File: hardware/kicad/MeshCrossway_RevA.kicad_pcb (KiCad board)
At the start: 2 copper layers, 0 parts

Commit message: Update Rev A KiCad PCB schematic and validated footprints
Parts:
- added BAT1: LiPo 3.7V 10000mAh 110x60x12, MeshCrossway:Battery_LiPo_10000mAh_110x60x12, B.Cu at (157.2, 94.2)
- added C1: 100nF, Capacitor_SMD:C_0603_1608Metric, B.Cu at (92.5, 71.0)
- added C10: 10uF, Capacitor_SMD:C_0805_2012Metric, B.Cu at (102.5, 103.5)
- added C2: 10uF, Capacitor_SMD:C_0805_2012Metric, B.Cu at (94.9, 71.0)
- added C3: 47uF DNP, Capacitor_SMD:C_1210_3225Metric, B.Cu at (102.0, 71.0)
- added C4: 100uF DNP, Capacitor_SMD:C_1210_3225Metric, B.Cu at (98.1, 71.0)
- added C5: 100nF, Capacitor_SMD:C_0603_1608Metric, B.Cu at (212.0, 71.5)
- added C6: 10uF, Capacitor_SMD:C_0805_2012Metric, B.Cu at (214.4, 71.5)
- added C7: 47uF DNP, Capacitor_SMD:C_1210_3225Metric, B.Cu at (221.5, 71.5)
- added C8: 100uF DNP, Capacitor_SMD:C_1210_3225Metric, B.Cu at (217.6, 71.5)
- added C9: 100nF, Capacitor_SMD:C_0603_1608Metric, B.Cu at (100.3, 103.5)
- added D1: Schottky, Diode_SMD:D_SOD-123, B.Cu at (98.5, 94.5)
- added D2: Schottky, Diode_SMD:D_SOD-123, B.Cu at (217.0, 94.5)
- added J1: Waveshare ESP32-S3-Touch-LCD-3.5 — J8, MeshCrossway:Waveshare_J8_Mating_2x16_P2.54mm, F.Cu at (157.2, 119.0)
- added J2: HOST DEBUG, Connector_PinHeader_2.54mm:PinHeader_1x04_P2.54mm_Vertical, F.Cu at (176.0, 128.5)
- added J5: BATTERY JST-PH 2.0, Connector_JST:JST_PH_B2B-PH-K_1x02_P2.00mm_Vertical, B.Cu at (221.0, 114.5)
- added JP1: A POWER SELECT, Connector_PinHeader_2.54mm:PinHeader_1x03_P2.54mm_Vertical, F.Cu at (216.5, 102.9)
- added JP2: A CURRENT LINK, Connector_PinHeader_2.54mm:PinHeader_1x02_P2.54mm_Vertical, F.Cu at (92.8, 94.5)
- added JP3: B POWER SELECT, Connector_PinHeader_2.54mm:PinHeader_1x03_P2.54mm_Vertical, F.Cu at (223.0, 102.9)
- added JP4: B CURRENT LINK, Connector_PinHeader_2.54mm:PinHeader_1x02_P2.54mm_Vertical, F.Cu at (222.2, 94.5)
- added R1: 47R, Resistor_SMD:R_0603_1608Metric, B.Cu at (147.0, 114.5)
- added R2: 47R, Resistor_SMD:R_0603_1608Metric, B.Cu at (149.5, 114.5)
- added R3: 47R, Resistor_SMD:R_0603_1608Metric, B.Cu at (157.0, 114.5)
- added R4: 47R, Resistor_SMD:R_0603_1608Metric, B.Cu at (159.0, 114.5)
- added R5: 0R, Resistor_SMD:R_0603_1608Metric, B.Cu at (142.5, 114.5)
- added R6: 4.7k DNP, Resistor_SMD:R_0603_1608Metric, B.Cu at (96.5, 103.5)
- added R7: 4.7k DNP, Resistor_SMD:R_0603_1608Metric, B.Cu at (98.4, 103.5)
- added TP1: TestPoint, TestPoint:TestPoint_Pad_D2.0mm, F.Cu at (108.9, 130.0)
- added TP10: TestPoint, TestPoint:TestPoint_Pad_D2.0mm, F.Cu at (129.4, 130.0)
- added TP2: TestPoint, TestPoint:TestPoint_Pad_D2.0mm, F.Cu at (114.1, 130.0)
- added TP3: TestPoint, TestPoint:TestPoint_Pad_D2.0mm, F.Cu at (134.5, 130.0)
- added TP4: TestPoint, TestPoint:TestPoint_Pad_D2.0mm, F.Cu at (98.7, 130.0)
- added TP5: TestPoint, TestPoint:TestPoint_Pad_D2.0mm, F.Cu at (88.5, 130.0)
- added TP6: TestPoint, TestPoint:TestPoint_Pad_D2.0mm, F.Cu at (103.8, 130.0)
- added TP7: TestPoint, TestPoint:TestPoint_Pad_D2.0mm, F.Cu at (124.3, 130.0)
- added TP8: TestPoint, TestPoint:TestPoint_Pad_D2.0mm, F.Cu at (93.6, 130.0)
- added TP9: TestPoint, TestPoint:TestPoint_Pad_D2.0mm, F.Cu at (119.2, 130.0)
- added U1: LOCAL 5V SOURCE — TBD, MeshCrossway:Module_LOCAL_5V_3Pin_Prototype, B.Cu at (220.0, 124.0)
- added U2: XIAO + Wio-SX1262, MeshCrossway:Module_XIAO_ESP32S3_WioSX1262_Socket, F.Cu at (97.4, 77.5)
- added U3: XIAO + Wio-SX1262, MeshCrossway:Module_XIAO_ESP32S3_WioSX1262_Socket, F.Cu at (217.1, 77.5)
- added U4: Uputronics MAX-M10S 3V, MeshCrossway:Module_Uputronics_MAX_M10S_3V_MECH_APPROX, F.Cu at (106.3, 110.0)

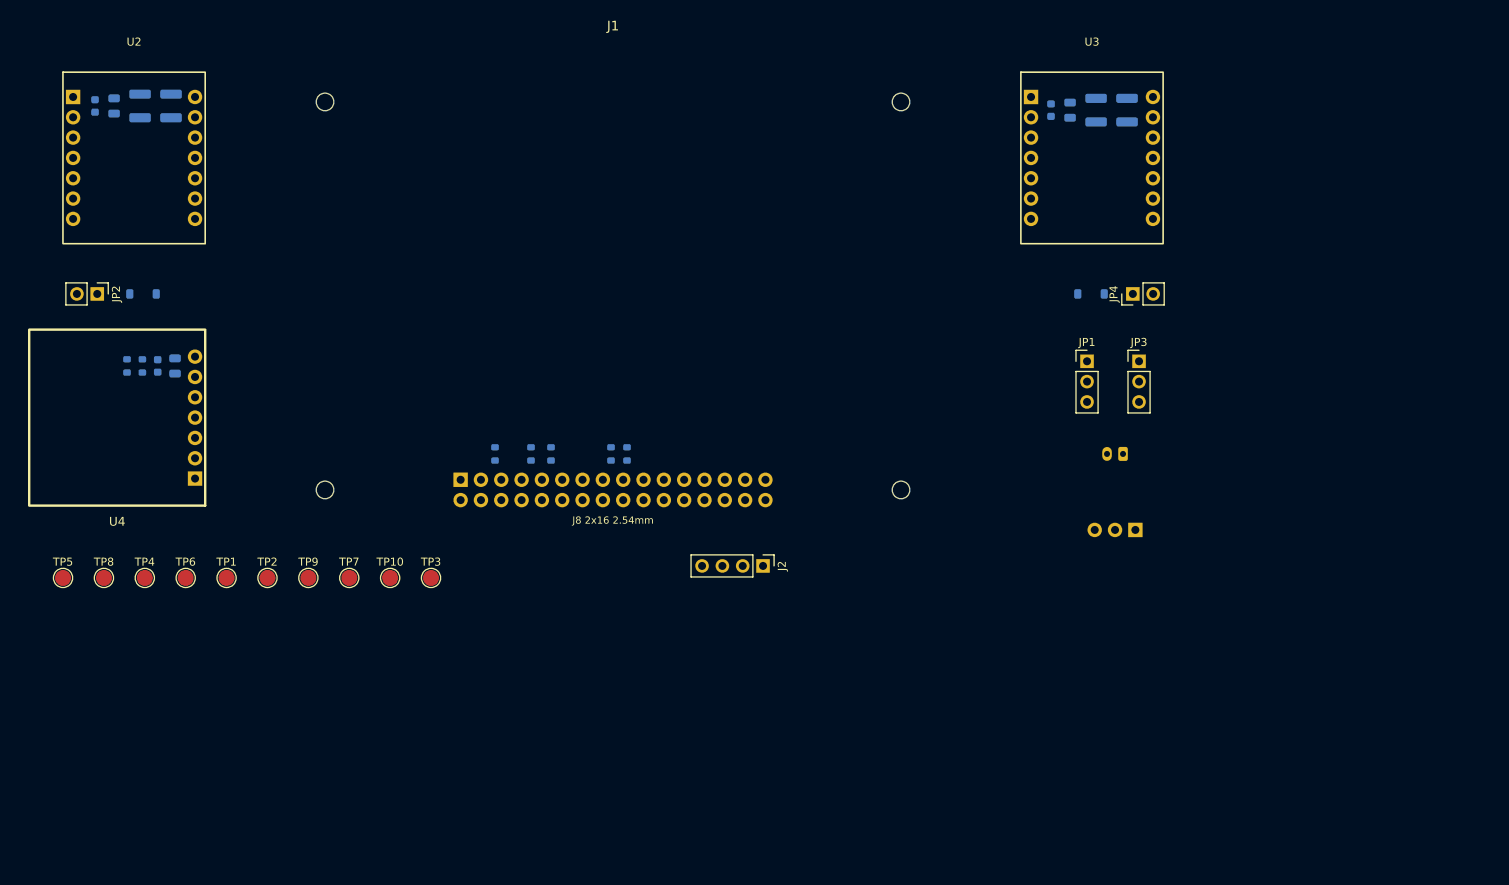
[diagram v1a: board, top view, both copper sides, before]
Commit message: Rework test points and PCB placement in KiCad RevA
Schematic: remove the UART test points (MC/MT_HOST_TX/RX, TP5-TP8) with their wires and labels. Rename and move the power test points to a single row: J85V, 5V, Ra5Vin, Rb5Vin, Ra3v3out, Rb3v3out. Reference designators are now descriptive instead of TPn.

PCB: sync to the schematic, with the renamed test points placed in a cluster near x=254-262, y=73-77. Reposition J1, J2, JP1, JP3, U4, the battery, and the decoupling caps and resistors on the back side. Rotate several parts, regroup the GNSS-related parts, and drop the stale KiLib_Generator properties.

Project: update the used_designators list.
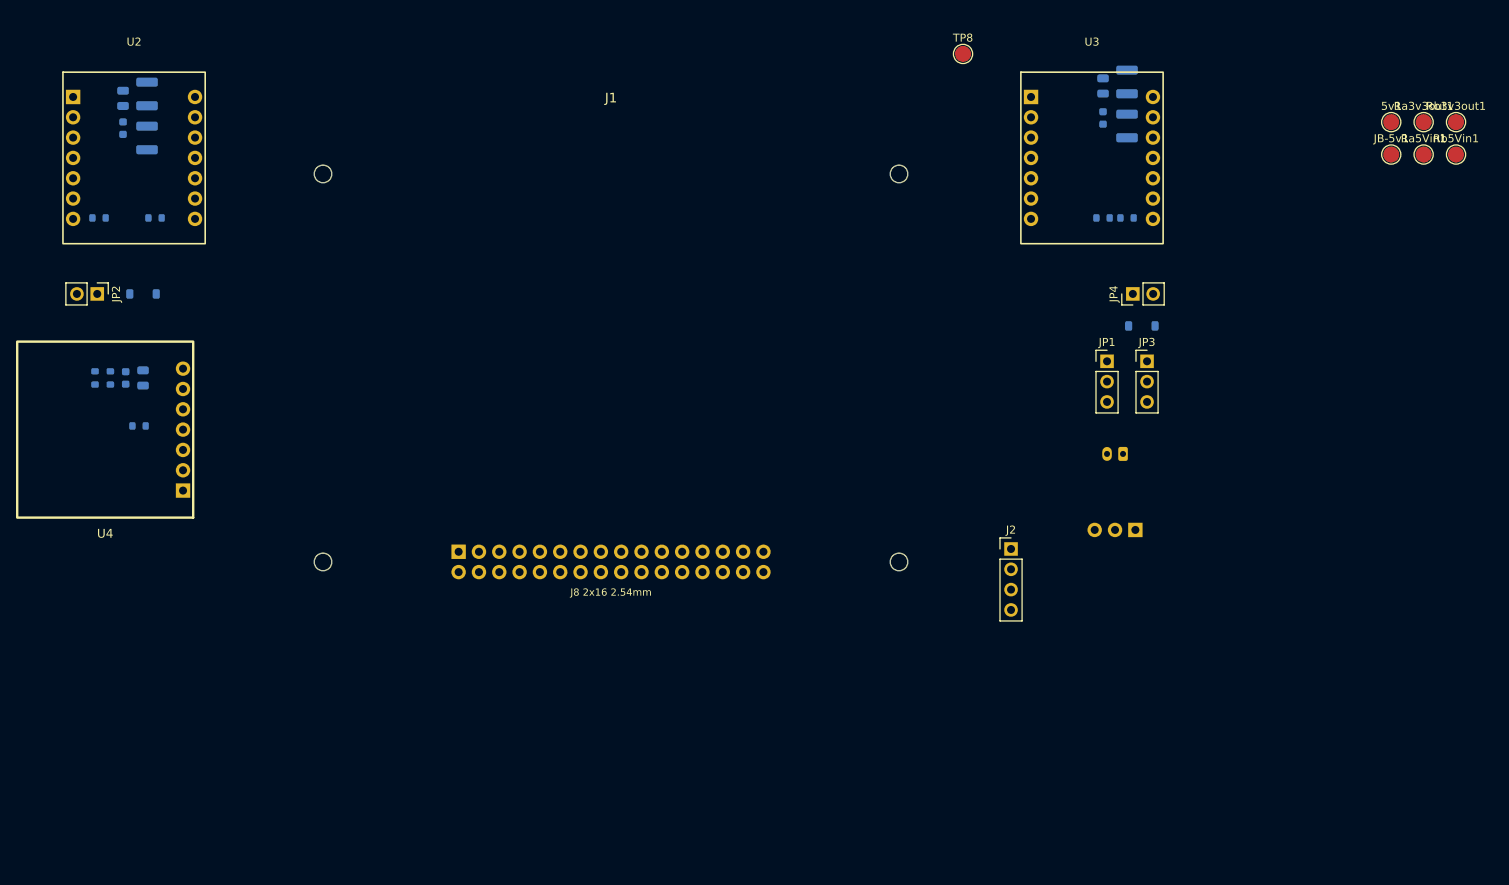
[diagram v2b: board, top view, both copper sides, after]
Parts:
- removed TP1, TP10, TP2, TP3, TP4, TP5, TP6, TP7, TP9: TestPoint, TestPoint:TestPoint_Pad_D2.0mm
- added 5v1: TestPoint, TestPoint:TestPoint_Pad_D2.0mm, F.Cu at (254.5, 73.0)
- added JB-5v1: TestPoint, TestPoint:TestPoint_Pad_D2.0mm, F.Cu at (254.5, 77.1)
- added Ra3v3out1: TestPoint, TestPoint:TestPoint_Pad_D2.0mm, F.Cu at (258.6, 73.0)
- added Ra5Vin1: TestPoint, TestPoint:TestPoint_Pad_D2.0mm, F.Cu at (258.6, 77.1)
- added Rb3v3out1: TestPoint, TestPoint:TestPoint_Pad_D2.0mm, F.Cu at (262.6, 73.0)
- added Rb5Vin1: TestPoint, TestPoint:TestPoint_Pad_D2.0mm, F.Cu at (262.6, 77.1)
- moved TP8 125.8 mm to (201.0, 64.5)
- moved R3 70.9 mm to (221.5, 85.0), turned to 0 degrees
- moved R4 66.4 mm to (218.5, 85.0), turned to 0 degrees
- moved R2 63.7 mm to (93.0, 85.0), turned to 0 degrees
- moved R1 55.5 mm to (100.0, 85.0), turned to 0 degrees
- moved R5 44.6 mm to (98.0, 111.0), turned to 180 degrees
- moved J2 31.1 mm to (207.0, 126.4), turned to 0 degrees
- moved J1 9.00 mm to (157.0, 128.0)
- moved D2 7.50 mm to (223.3, 98.5)
- moved C5 6.57 mm to (218.5, 72.5)
- moved C6 5.11 mm to (218.5, 68.5), turned to 90 degrees
- moved C3 5.00 mm to (99.0, 75.0)
- moved C1 4.47 mm to (96.0, 73.8)
- moved C8 4.34 mm to (221.5, 73.5)
- moved C10 4.27 mm to (98.5, 105.0)
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
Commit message: Link PCB test points to schematic TP symbols
Replaced the old ad-hoc test point footprints (Ra3v3out1, Rb5Vin1, 5v1, etc.) in the PCB with TP1-TP10 footprints tied to the schematic symbols via their paths. The new footprints carry net-named values and are placed in a cluster at the board's lower-left. Added the missing symbol path on the MC_HOST_RX footprint and on one other footprint.

In the schematic, moved the 5V/3V3 test point row up and left and added MT/MC host TX/RX test points with their labels and wires. Reformatted the existing TP symbols to the standard KiCad layout. Cleared the stale used_designators list in the project file.
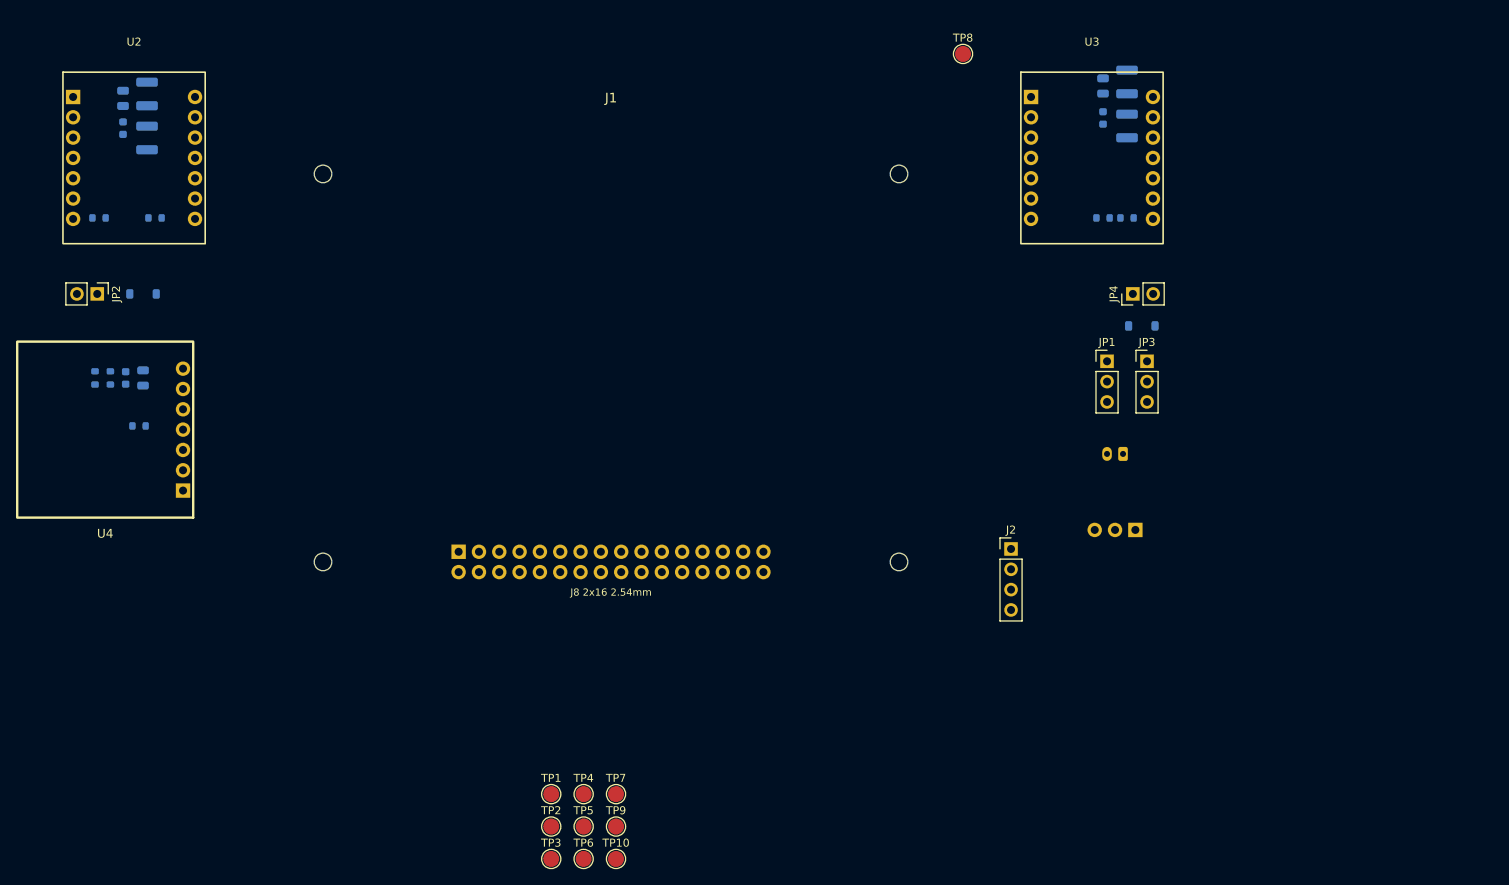
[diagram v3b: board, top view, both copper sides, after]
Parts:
- removed 5v1, JB-5v1, Ra3v3out1, Ra5Vin1, Rb3v3out1, Rb5Vin1: TestPoint, TestPoint:TestPoint_Pad_D2.0mm
- added TP1: J8_5V, TestPoint:TestPoint_Pad_D2.0mm, F.Cu at (149.5, 157.0)
- added TP10: B_3V3_OUT, TestPoint:TestPoint_Pad_D2.0mm, F.Cu at (157.6, 165.1)
- added TP2: LOCAL_5V, TestPoint:TestPoint_Pad_D2.0mm, F.Cu at (149.5, 161.1)
- added TP3: RADIO_A_5V, TestPoint:TestPoint_Pad_D2.0mm, F.Cu at (149.5, 165.1)
- added TP4: RADIO_B_5V, TestPoint:TestPoint_Pad_D2.0mm, F.Cu at (153.6, 157.0)
- added TP5: MT_HOST_TX, TestPoint:TestPoint_Pad_D2.0mm, F.Cu at (153.6, 161.1)
- added TP6: MT_HOST_RX, TestPoint:TestPoint_Pad_D2.0mm, F.Cu at (153.6, 165.1)
- added TP7: MC_HOST_TX, TestPoint:TestPoint_Pad_D2.0mm, F.Cu at (157.6, 157.0)
- added TP9: A_3V3_OUT, TestPoint:TestPoint_Pad_D2.0mm, F.Cu at (157.6, 161.1)
- TP8: value TestPoint -> MC_HOST_RX

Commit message: Route RevA PCB, add netclasses and board outline
Advance the RevA layout from placement to routing.

PCB:
- Add a 2-layer stackup (FR4, 1.6mm).
- Replace the Margin rectangle with an Edge.Cuts outline (85,60.5 to 229,137).
- Add GND copper pour zones on F.Cu and B.Cu.
- Route power (BAT, 5V, 3V3), UART and I2C/PPS nets.
- Re-place the GNSS module, battery, JST connector, JP1/JP3 headers, J2, the 10uF/0603 caps and the series/pull-up resistors.
- Move D1, D2, JP2 and TP3/TP4 to new positions.
- Remove the unused TP1/TP2/TP5-TP10 test pads.

Project:
- Add netclasses GND, PWR_3V3, PWR_5V_MAIN, PWR_5V_RADIO, PWR_BAT and SIGNAL, with width, via and clearance settings, and net patterns assigning the power nets to them.
- Add track width and via dimension presets.
- Change the default pad size to 1.8mm with a 1.0mm drill.
- Change the Default netclass track width to 0.25mm.
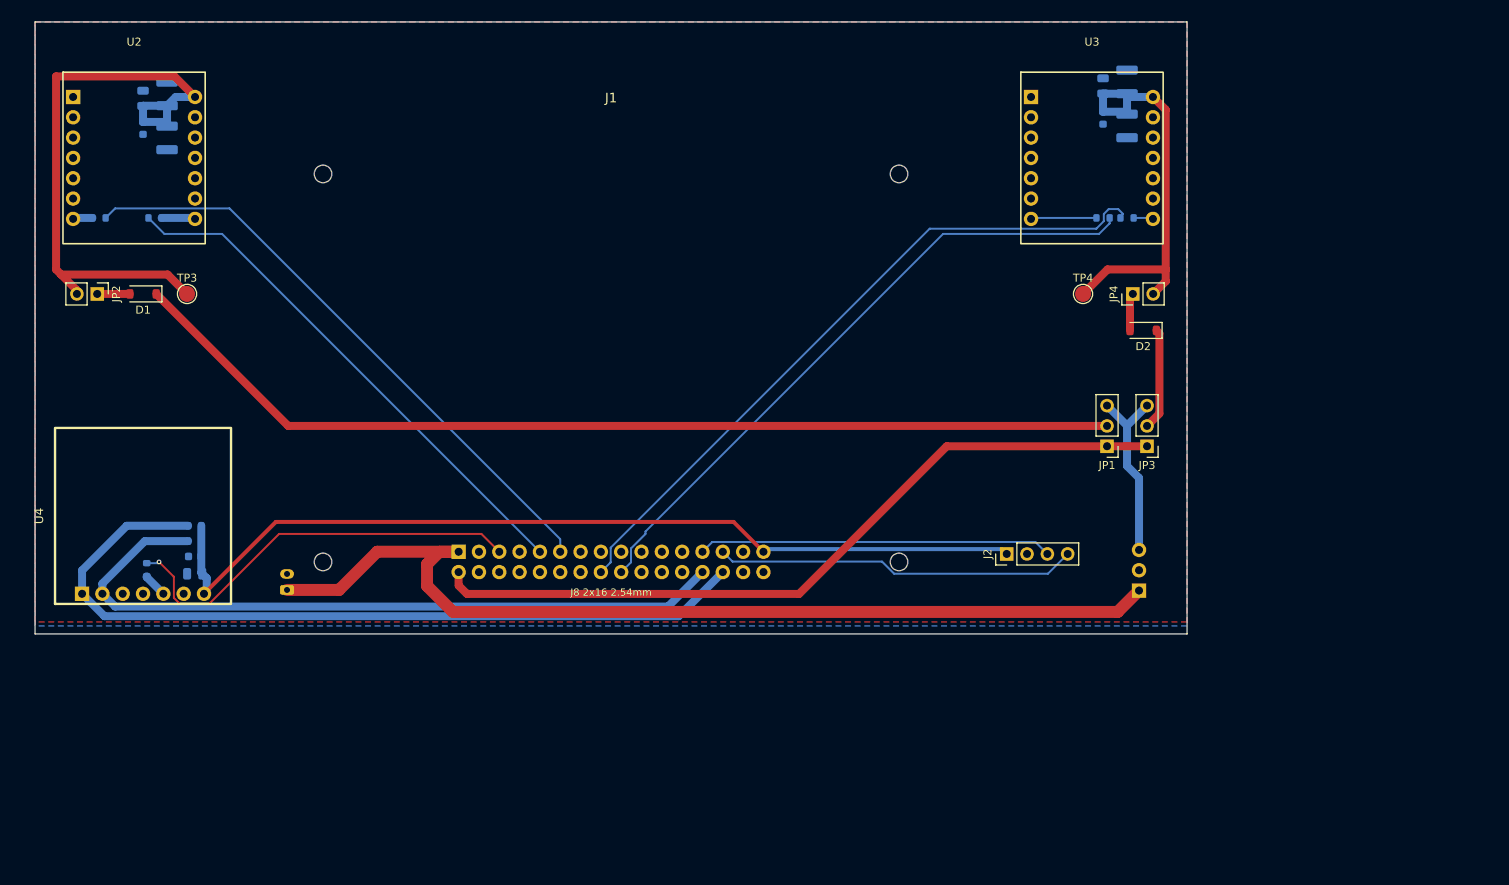
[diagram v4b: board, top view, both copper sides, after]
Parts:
- removed TP1: J8_5V, TestPoint:TestPoint_Pad_D2.0mm
- removed TP10: B_3V3_OUT, TestPoint:TestPoint_Pad_D2.0mm
- removed TP2: LOCAL_5V, TestPoint:TestPoint_Pad_D2.0mm
- removed TP5: MT_HOST_TX, TestPoint:TestPoint_Pad_D2.0mm
- removed TP6: MT_HOST_RX, TestPoint:TestPoint_Pad_D2.0mm
- removed TP7: MC_HOST_TX, TestPoint:TestPoint_Pad_D2.0mm
- removed TP8: MC_HOST_RX, TestPoint:TestPoint_Pad_D2.0mm
- removed TP9: A_3V3_OUT, TestPoint:TestPoint_Pad_D2.0mm
- D1, D2: moved to F.Cu
- moved J5 105.9 mm to (116.5, 131.5), turned to 90 degrees
- moved TP4 88.4 mm to (216.0, 94.5)
- moved TP3 84.0 mm to (104.0, 94.5)
- moved C10 25.3 mm to (105.0, 129.5), turned to 180 degrees
- moved C9 23.9 mm to (105.0, 127.3), turned to 180 degrees
- moved R7 23.0 mm to (105.0, 125.4), turned to 180 degrees
- moved U4 22.7 mm to (98.5, 133.2), turned to 90 degrees
- moved R6 22.3 mm to (105.0, 123.5), turned to 180 degrees
- moved R5 18.0 mm to (99.0, 129.0), turned to 90 degrees
- moved JP1 10.6 mm to (219.0, 113.5), turned to 180 degrees
- moved JP3 10.6 mm to (224.0, 113.5), turned to 180 degrees
- moved U1 5.87 mm to (223.0, 129.0), turned to 90 degrees
- moved C1 2.50 mm to (98.5, 73.8)
- moved C2 2.50 mm to (98.5, 70.0)
- moved C3 2.50 mm to (101.5, 75.0)
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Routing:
- net Net-(D1-A): track 0.00 -> 125.7 mm
- net /BAT: track 0.00 -> 122.2 mm
- net /J8_3V3: track 0.00 -> 115.4 mm
- net /GNSS_SDA: track 0.00 -> 102.0 mm
- net /J8_5V: track 0.00 -> 95.8 mm
- net /GNSS_SCL: track 0.00 -> 91.6 mm
- net /MC_HOST_TX: track 0.00 -> 86.5 mm
- net /MC_HOST_RX: track 0.00 -> 81.0 mm
- net /RADIO_A_5V: track 0.00 -> 78.2 mm
- net /MT_HOST_RX: track 0.00 -> 76.0 mm
- net /MT_HOST_TX: track 0.00 -> 66.2 mm
- net /GNSS_PPS: track 0.00 -> 52.4 mm, vias 0 -> 1
- net /RADIO_B_5V: track 0.00 -> 52.0 mm
- net /HOST_TXD: track 0.00 -> 45.3 mm
- net /HOST_RXD: track 0.00 -> 44.2 mm
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- added copper zone on B.Cu, net /GND
- added copper zone on F.Cu, net /GND
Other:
- board outline added: 144 x 76.5 mm
